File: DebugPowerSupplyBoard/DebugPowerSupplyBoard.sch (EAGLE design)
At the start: 7 parts, among them IC1 LD117AV33, IC2 7805T

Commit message: Progress was made
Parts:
- added J1: (no value), CustomEuroCard:VG96KB
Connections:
- new net A1: J1.A1, J2.A1
- new net A10: J1.A10, J2.A10
- new net A2: J1.A2, J2.A2
- new net B10: J1.B10, J2.B10
- new net C10: J1.C10, J2.C10
- new net N$10: J1.A17, J2.A17
- new net N$100: J1.A31, J2.A31
- new net N$101: J1.B31, J2.B31
- new net N$102: J1.C31, J2.C31
- new net N$103: J1.A32, J2.A32
- new net N$104: J1.B32, J2.B32
- new net N$105: J1.C32, J2.C32
- new net N$11: J1.B17, J2.B17
- new net N$12: J1.C17, J2.C17
- new net N$13: J1.A18, J2.A18
- new net N$14: J1.B18, J2.B18
- new net N$16: J1.C18, J2.C18
- new net N$18: J1.A19, J2.A19
- new net N$19: J1.B19, J2.B19
- new net N$20: J1.C19, J2.C19
- new net N$21: J1.A20, J2.A20
- new net N$22: J1.B20, J2.B20
- new net N$23: J1.C20, J2.C20
- new net N$25: J1.A21, J2.A21
- new net N$39: J1.B21, J2.B21
- new net N$4: J1.A15, J2.A15
- new net N$40: J1.C21, J2.C21
- new net N$44: J1.A22, J2.A22
- new net N$45: J1.B22, J2.B22
- new net N$47: J1.C22, J2.C22
- new net N$49: J1.A23, J2.A23
- new net N$5: J1.B15, J2.B15
- new net N$50: J1.B23, J2.B23
- new net N$51: J1.C23, J2.C23
- new net N$52: J1.A24, J2.A24
- new net N$53: J1.B24, J2.B24
- new net N$54: J1.C24, J2.C24
- new net N$55: J1.A25, J2.A25
- new net N$56: J1.B25, J2.B25
- new net N$57: J1.C25, J2.C25
- new net N$58: J1.A26, J2.A26
- new net N$6: J1.C15, J2.C15
- new net N$67: J1.B26, J2.B26
- new net N$69: J1.C26, J2.C26
- new net N$7: J1.A16, J2.A16
- new net N$70: J1.A27, J2.A27
- new net N$79: J1.B27, J2.B27
- new net N$8: J1.B16, J2.B16
- new net N$86: J1.C27, J2.C27
- new net N$87: J1.A28, J2.A28
- new net N$89: J1.B28, J2.B28
- new net N$9: J1.C16, J2.C16
- new net N$90: J1.C28, J2.C28
- new net N$92: J1.A29, J2.A29
- new net N$94: J1.B29, J2.B29
- new net N$95: J1.C29, J2.C29
- new net N$97: J1.A30, J2.A30
- new net N$98: J1.B30, J2.B30
- new net N$99: J1.C30, J2.C30
- net +3V3: now also J1.B1, J1.C1
- net +5V: now also J1.C4
- net +5V_DIFF: now also J1.A8
- net +7V_DIFF: now also J1.A9
- net -5V_DIFF: now also J1.C8
- net -7V_DIFF: now also J1.C9
- net CHARGE_PROBE_0: now also J1.A14
- net CHARGE_PROBE_1: now also J1.B14
- net CONDUCTIVITY_ENABLE: now also J1.C14
- net GND: now also J1.A5, J1.A6, J1.A7, J1.B11, J1.B12, J1.B13
- net GND_3V3: now also J1.B2, J1.C2
- net GND_5V: now also J1.C3
- net GND_5V_DIFF: now also J1.B8
- net GND_7V_DIFF: now also J1.B9
- net GND_TEMP: now also J1.B3
- net I_1_H: now also J1.C5
- net I_1_L: now also J1.B5
- net I_2_H: now also J1.C6
- net I_2_L: now also J1.B6
- net I_3_H: now also J1.C7
- net I_3_L: now also J1.B7
- net PROBE_DIFF_HOR: now also J1.A13
- net PROBE_DIFF_VERT: now also J1.C13
- net PROBE_HOR_1_RIGHT: now also J1.A11
- net PROBE_HOR_2_LEFT: now also J1.A12
- net PROBE_VERT_1_UP: now also J1.C11
- net PROBE_VERT_2_DOWN: now also J1.C12
- net TEMP_1: now also J1.B4
- net TEMP_2: now also J1.A4
- net TEMP_3: now also J1.A3

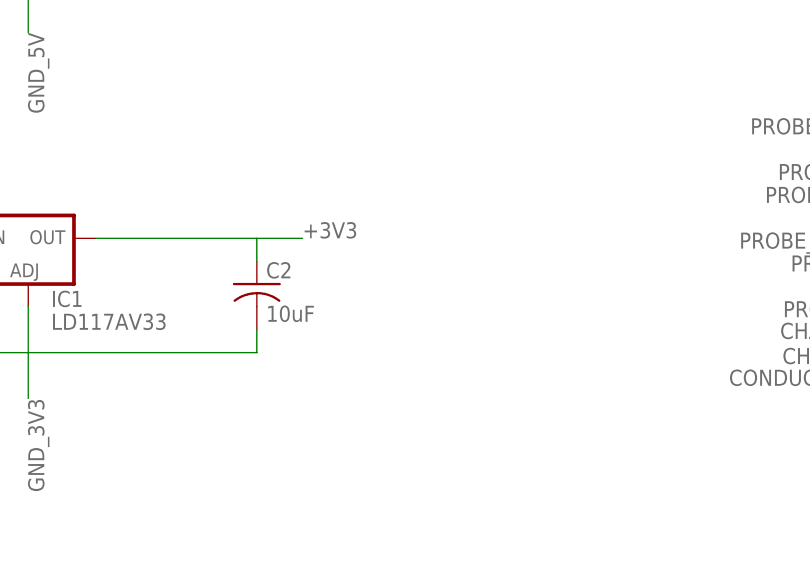
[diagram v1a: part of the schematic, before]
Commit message: Changed the capacitors used to be ones which are readily avaliable from DigiKey
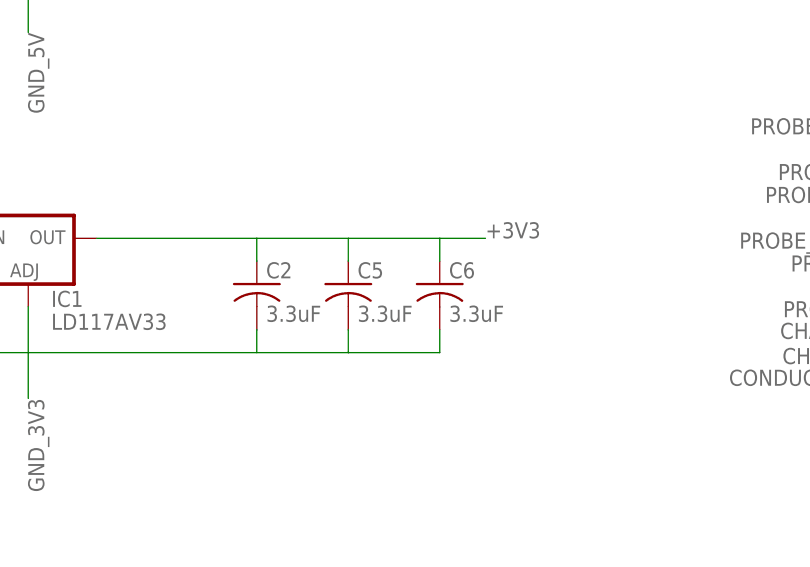
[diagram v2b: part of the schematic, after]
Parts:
- added C5, C6: 3.3uF, rcl:C-US050-055X075
- C2: value 10uF -> 3.3uF; device rcl:C-US050-025X075 -> rcl:C-US050-055X075
- C3: device rcl:C-US050-025X075 -> rcl:C-US050-035X075
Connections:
- net +3V3: now also C5.1, C6.1
- net GND_3V3: now also C5.2, C6.2
